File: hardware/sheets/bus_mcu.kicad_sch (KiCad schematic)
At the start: 38 parts, among them M1 Core2350B (0MB PSRAM), U10 74HCT163, U11 74HCT163, U12 74HCT165, U13 74LVC245A, U14 74HCT244, U15 74HCT244, U16 74HCT244, U17 74HCT04, U2 74LVC245A, U3 74LVC245A, U4 74LVC245A, U5 74LVC245A, U6 74LVC245A, U7 74HCT163, U8 74HCT163, U9 74HCT163

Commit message: Fix all medium design-review findings (M1-M8)
- M1: Supervisor link moved to GPIO4/5 (real UART1 pair); POST -> GPIO6-15
- M2: CNT_RUN = LD0.LD1.LD2 gates every '163 CEP (load-cascade hazard)
- M3: ~WR / IO-M pruned to cpu_core-internal; DRQ2/3 pulled + noted;
  doc S5.2 "as built: 48/48" + S16 updated
- M4: true XT-IDE rev-2 map (A0<->A3 swap): data 0x300, latch 0x301,
  CS1 0x307/0x30F, drive DA0 = bus A3 - matches XTIDE UB "rev 2" type
- M5: COM4 -> bus IRQ2 line (IRQ9 via AT redirect); IRQ10/11/14/15 marked
  off-header; ~REFRESH added to mxbus ISA_CTRL; questions-sidecar superseded
- M6: card_isatest clock tree on unswitched V5RAW (spec S8)
- M7: card_isatest IRQ2-8/DRQ1-3 idle pull-downs (spec S4/S9)
- M8: com_port JP1 selects 16550 RX source (DB9 vs TTL console); 5V note

Rebuilt motherboard + cards; structural ERC = 0; netlist-verified.
Fix log in hardware/notes/design-review-2026-07-03.md (batch 3).

Co-Authored-By: Claude Fable 5 <noreply@anthropic.com>
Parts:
- added R14, R15: 10k, symbol Device:R
- added U18: 74HCT08, symbol mini-xt:74HCT08
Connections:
- net +5V: now also U18.14 (VCC); no longer U10.7 (CEP), U11.7 (CEP), U7.7 (CEP), U8.7 (CEP), U9.7 (CEP)
- net CNT_LD0: now also U18.1 (P1)
- net CNT_LD1: now also U18.2 (P2)
- net CNT_LD2: now also U18.5 (P5)
- net DRQ2: now also R14.2
- net DRQ3: now also R15.2
- net GND: now also R14.1, R15.1, U18.10 (P10), U18.12 (P12), U18.13 (P13), U18.7 (GND), U18.9 (P9)
- new net CNT_LD01: U18.3 (P3), U18.4 (P4)
- new net CNT_RUN: U10.7 (CEP), U11.7 (CEP), U18.6 (P6), U7.7 (CEP), U8.7 (CEP), U9.7 (CEP)
- no-connect marks 50 -> 52
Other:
- note added: "DMA ch2/3 + raw ~WR/IO-M are NOT wired to the MCU (48-GPIO budget, S5.2): DACK2/3 parked high, DRQ2/3 low. First candidates for a second '165/'595 if sidecar DMA is ever needed."

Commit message: JLCPCB sourcing pass: verify pinouts, LCSC part numbers, SMD build
Custom-symbol verification (open-questions Q5 resolved):
- MAX3241 symbol was wrong on nearly every pin and used MAX3243-style
  control names; regenerated to the real SSOP-28 pinout (SHDN#/EN#/
  R1OUTB/R2OUTB) and com_port rewired -- EN# must be GROUNDED (the old
  ~FORCEON-high would have disabled the receivers on real silicon)
- DS12C887 symbol wrong on 4 pins (DS=17, RESET#=18, IRQ#=19, SQW=23)

Sourcing (every part checked against the JLC DB; ~45 line items):
- New tools/parts.py maps (lib_id, value) -> LCSC; build.py applies it as
  an 'LCSC Part Num' property on every component (384 across the project)
- Sheets stay generic; stock-forced substitutions bound in the map:
  '374->'574 (parallel rewired), '163->'161, '157->HC157 (+HCT-buffered
  3.3V selects, I0/I1 swapped), '02->HC02, TCM809->MCP809, 2N3904->MMBT3904
- bus_mcu address counters moved to the 3.3V domain (HC161 on 3V3_BUS,
  loaded from MCU-side MD0-7; HCT244s read the 3.3V outputs at TTL Vih)
- 14.318 XOs are 3.3V-only parts: powered from 3V3, squared up via spare
  HCT gates (cpu_core U13, card_isatest U19)
- COM baud reference is now a 1.8432MHz crystal on the 16C550's XIN/XOUT
  (3.3V-only oscillators vs a 5V-only soft card)
- Supervisor QSPI header replaced with a real W25Q128JVSIQ
- Socket policy (fab installs sockets): V20 DIP-40, SRAM DIP-32 (no 5V
  512Kx8 SRAM at JLC at all), DS12C887 DIP-24, female headers for modules

Docs: CLAUDE.md fabrication-constraints section (SMD, 100x100mm, generic-
symbols rule, voltage-domain rule); README + hardware/README fab notes;
notes/jlcpcb-sourcing.md (decisions, thin-stock flags, not-at-JLC list);
stale questions-sidecar.md collapsed to its supersession record.

Rebuilt motherboard + cards: structural ERC 0, byte-identical rebuilds.

Co-Authored-By: Claude Fable 5 <noreply@anthropic.com>
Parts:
- removed C1: 100nF, symbol Device:C
- removed R2: 10k, symbol Device:R
- added C10: 100nF, symbol Device:C
- added R15: 10k, symbol Device:R
- added U17: 74HCT04, symbol mini-xt:74HCT04
- C1: renamed from C2; LCSC Part Num (none) -> C14663
- C11: renamed from U17; value 74HCT04 -> 100nF; symbol mini-xt:74HCT04 -> Device:C; LCSC Part Num (none) -> C14663
- C2: renamed from C3; value 10uF -> 100nF; LCSC Part Num (none) -> C14663
- C3: renamed from C6; value 100nF -> 10uF; LCSC Part Num (none) -> C15850
- C6: renamed from C7; LCSC Part Num (none) -> C14663
- C7: renamed from C8; LCSC Part Num (none) -> C14663
- C8: renamed from C9; LCSC Part Num (none) -> C14663
- C9: renamed from C10; LCSC Part Num (none) -> C14663
- M1: LCSC Part Num (none) -> C2897411
- R1: LCSC Part Num (none) -> C25804
- R10: renamed from R11; LCSC Part Num (none) -> C25804
- R11: renamed from R12; LCSC Part Num (none) -> C25804
- R12: renamed from R13; LCSC Part Num (none) -> C25804
- R13: renamed from R14; LCSC Part Num (none) -> C25804
- R14: renamed from R15; LCSC Part Num (none) -> C25804
- R2: renamed from R3; LCSC Part Num (none) -> C25804
- R3: renamed from R4; LCSC Part Num (none) -> C25804
- R4: renamed from R5; LCSC Part Num (none) -> C25804
- R5: renamed from R6; LCSC Part Num (none) -> C25804
- R6: renamed from R7; LCSC Part Num (none) -> C25804
- R7: renamed from R8; LCSC Part Num (none) -> C25804
- R8: renamed from R9; LCSC Part Num (none) -> C25804
- R9: renamed from R10; LCSC Part Num (none) -> C25804
- U10, U11, U7, U8, U9: value 74HCT163 -> 74HC161; LCSC Part Num (none) -> C5610
- U12: LCSC Part Num (none) -> C456131
- U13, U2, U3, U4, U5, U6: LCSC Part Num (none) -> C6082
- U14, U15, U16: LCSC Part Num (none) -> C5978
- U18: value 74HCT08 -> 74HC08; LCSC Part Num (none) -> C5593
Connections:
- net 3V3_BUS is gone; now on net GND: C1.1, C2.1, C3.1, C6.1, M1.50 (3V3), U13.1 (A->B), U13.20 (VCC), U2.20 (VCC), U3.20 (VCC), U4.20 (VCC), U5.20 (VCC), U6.20 (VCC)
- net +3V3: now also C8.1; no longer C7.1
- net +5V: now also R13.1, R3.1, C10.1, U17.14 (VCC); no longer C11.14 (VCC), C8.1, C9.1, R11.1, U10.1 (~{MR}), U10.16 (VCC), U11.1 (~{MR}), U11.16 (VCC), U18.14 (VCC), U7.1 (~{MR}), U7.10 (CET), U7.16 (VCC), U8.1 (~{MR}), U8.16 (VCC), U9.1 (~{MR}), U9.16 (VCC)
- net D0: no longer U11.3 (D0), U7.3 (D0), U9.3 (D0)
- net D1: no longer U11.4 (D1), U7.4 (D1), U9.4 (D1)
- net D2: no longer U11.5 (D2), U7.5 (D2), U9.5 (D2)
- net D3: no longer U11.6 (D3), U7.6 (D3), U9.6 (D3)
- net D4: no longer U10.3 (D0), U8.3 (D0)
- net D5: no longer U10.4 (D1), U8.4 (D1)
- net D6: no longer U10.5 (D2), U8.5 (D2)
- net D7: no longer U10.6 (D3), U8.6 (D3)
- net DRQ2: now also R14.2; no longer R13.2
- net DRQ3: now also R15.2; no longer R14.2
- net GND: now also C11.1, C11.2, C7.1, C9.1, R11.1, U10.1 (~{MR}), U10.16 (VCC), U11.1 (~{MR}), U11.16 (VCC), U18.14 (VCC), U7.1 (~{MR}), U7.10 (CET), U7.16 (VCC), U8.1 (~{MR}), U8.16 (VCC), U9.1 (~{MR}), U9.16 (VCC), C10.2, R15.1, U17.7 (GND); no longer C11.7 (GND), R13.1, R3.1
- net HLDA: now also U17.1 (P1); no longer C11.1 (P1)
- net IOCHRDY: now also R2.2
- net IRQ2: now also R4.2; no longer R3.2
- net IRQ3: now also R5.2; no longer R4.2
- net IRQ4: now also R6.2; no longer R5.2
- net IRQ5: now also R7.2; no longer R6.2
- net IRQ6: now also R8.2; no longer R7.2
- net IRQ7: now also R9.2; no longer R8.2
- net IRQ8: now also R10.2; no longer R9.2
- net IRQ9: now also R11.2; no longer R10.2
- net MD0: now also U11.3 (D0), U7.3 (D0), U9.3 (D0)
- net MD1: now also U11.4 (D1), U7.4 (D1), U9.4 (D1)
- net MD2: now also U11.5 (D2), U7.5 (D2), U9.5 (D2)
- net MD3: now also U11.6 (D3), U7.6 (D3), U9.6 (D3)
- net MD4: now also U10.3 (D0), U8.3 (D0)
- net MD5: now also U10.4 (D1), U8.4 (D1)
- net MD6: now also U10.5 (D2), U8.5 (D2)
- net MD7: now also U10.6 (D3), U8.6 (D3)
- net ~{DACK2}: now also R12.2; no longer R11.2
- net ~{DACK3}: now also R13.2; no longer R12.2
- net ~{HLDA}: now also U17.2 (P2); no longer C11.2 (P2)
- net ~{IOCHCK}: now also R3.2; no longer R2.2
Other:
- moved on the sheet: C1, C2, C3, C6, C7, C8, C9, R10, R11, R12, R13, R14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

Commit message: Design review 2026-07-11: rail protection, decoupling, wiring fixes
Protection:
- Sidecar +5V now feeds through a 2A polyfuse into +5V_ISA with an
  SMBJ5.0A clamp + 22uF bulk (a faulted ISA card trips its own fuse
  instead of dropping the board; back-fed voltage is clamped).
- USB-C VBUS enters through a 3A polyfuse with an SMBJ5.0A on +5V
  (backstop for the CFG1 9-20V failure mode). CH224K gains a 1uF VDD
  cap; its PG routes to Supervisor GPIO16 as PD_PG. Buck output
  doubled to 2x22uF, 10uF at VIN, extra rail bulk.
- Supervisor USB-A host port: 27R series termination (RP2040
  requirement), USBLC6-2SC6 ESD array, 100uF VBUS bulk.
- Video: HDMI +5V fused (500mA), HPD sensed on GPIO41, 100R series on
  VGA sync. TMDS ESD array deferred to layout (no symbol).
- card_isatest: V5RAW bulk, Q1 gate soft-start cap, TVS on DUT rail.

Wiring fixes:
- SPKR had no driver anywhere (netlist: 1 node). Bus MCU GPIO22
  reassigned from the diagnostics-only bus-CLK sense to SPKR; bus_mcu
  drops CLK from its interface. Doc 5.2 updated.
- bus_mcu C8 decoupled +3V3, a rail that sheet never uses -> 3V3_BUS.
- Storage IRQ5 was push-pull (permanently driven when idle) -> 2N7002
  + gated '125 tri-state, same convention as the LPT IRQ7 stage.
- MAX3241 pump caps resized to the 5V datasheet values (47nF/330nF).
- LPT DB25 status inputs get 4.7k pull-ups (floated with no printer).
- Audio line-out gets a 100R series isolator before the jack.

Best practices:
- Decoupling to ~1x100nF per IC on every sheet + bulk per board
  (cpu_core 7->16 incl. the naked 3.3V oscillator, storage 4->11,
  parallel 6->13, rtc/com/video/bus_mcu/card_isatest similar).
- All floating spare CMOS inputs tied ('00/'74/'157/'02/'04/'125
  sections across cpu_core, bus_mcu, rtc, storage, card_isatest).

Sourcing: new parts mapped in parts.py with JLC-verified LCSC numbers;
Power_Protection lib registered in the tools; TPS563200 stock alert
(4 pcs left at JLC) flagged in parts.py + jlcpcb-sourcing.md. All
decisi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
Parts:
- removed C1: 100nF, symbol Device:C
- removed R2: 10k, symbol Device:R
- added C10, C12, C13, C14, C15, C16, C17: 100nF, symbol Device:C
- added R15: 10k, symbol Device:R
- C2: renamed from C3; value 10uF -> 100nF; LCSC Part Num C15850 -> C14663
- C3: renamed from C6; value 100nF -> 10uF; LCSC Part Num C14663 -> C15850
- renumbered C2 to C1, C7 to C6, C8 to C7, C9 to C8, C10 to C9, R11 to R10, R12 to R11, R13 to R12, R14 to R13, R15 to R14, R3 to R2, R4 to R3, R5 to R4, R6 to R5, R7 to R6, R8 to R7, R9 to R8, R10 to R9
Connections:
- net +3V3 is gone; now on net GND: C7.1
- net +5V: now also R13.1, R3.1, C10.1, C12.1, C13.1, C14.1, C15.1; no longer C9.1, R11.1
- net DRQ2: now also R14.2; no longer R13.2
- net DRQ3: now also R15.2; no longer R14.2
- net GND: now also C9.1, R11.1, U17.11 (P11), U17.13 (P13), U17.3 (P3), U17.5 (P5), U17.9 (P9), C10.2, C12.2, C13.2, C14.2, C15.2, C16.1, C16.2, C17.1, C17.2, R15.1; no longer R13.1, R3.1
- net IOCHRDY: now also R2.2
- net IRQ2: now also R4.2; no longer R3.2
- net IRQ3: now also R5.2; no longer R4.2
- net IRQ4: now also R6.2; no longer R5.2
- net IRQ5: now also R7.2; no longer R6.2
- net IRQ6: now also R8.2; no longer R7.2
- net IRQ7: now also R9.2; no longer R8.2
- net IRQ8: now also R10.2; no longer R9.2
- net IRQ9: now also R11.2; no longer R10.2
- net ~{DACK2}: now also R12.2; no longer R11.2
- net ~{DACK3}: now also R13.2; no longer R12.2
- net ~{IOCHCK}: now also R3.2; no longer R2.2
- net CLK renamed SPKR
- no-connect marks 52 -> 47
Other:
- moved on the sheet: C1, C2, C3, C6, C7, C8, C9, R10, R11, R12, R13, R14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

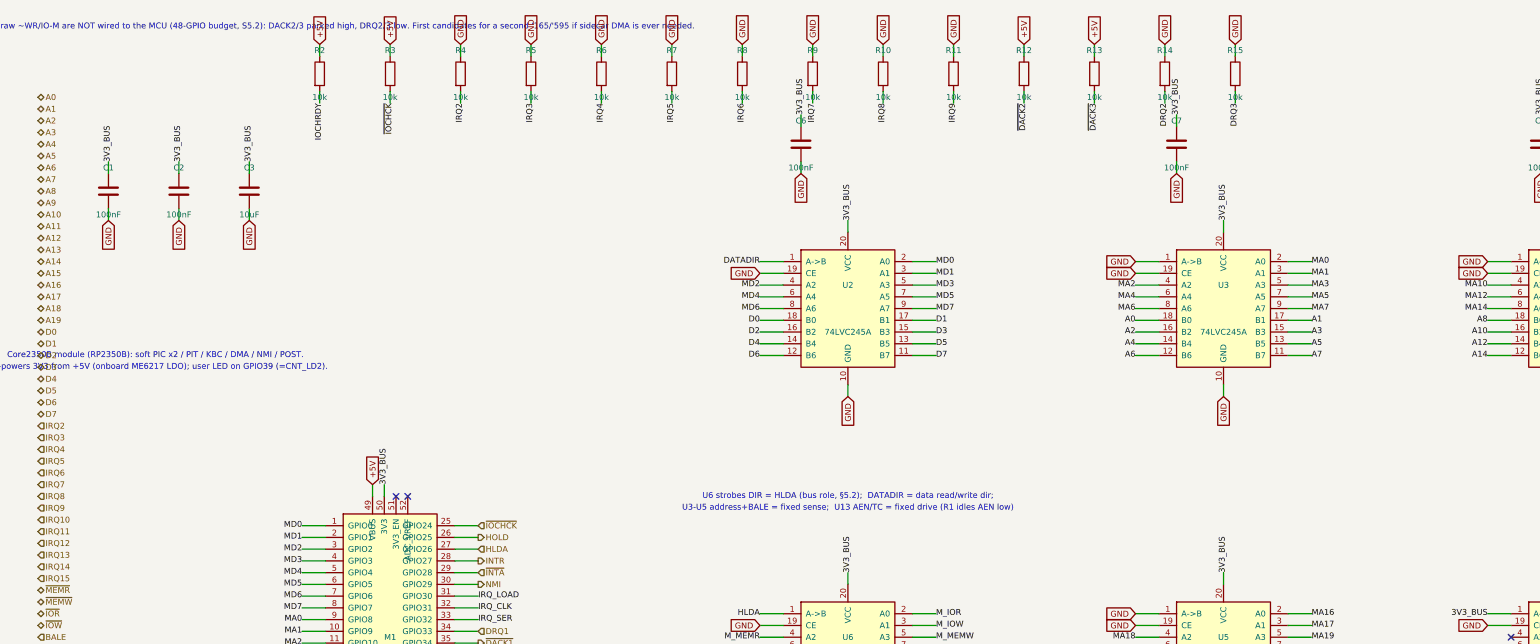
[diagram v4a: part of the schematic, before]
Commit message: Core2350B sites: VBUS diode-OR + Hi-Z shifter parking
The Waveshare Core2350B has NO diode between its on-module USB connector
and its VBUS pin (vendor schematic, hardware/Core2350B.pdf) -- with both
module sites tied straight to +5V, plugging a PC in for firmware flashing
would back-power the whole board (board off) or parallel two hard 5V
supplies (board on).

- D1 (SS34) per site, Pico-style: +5V -> anode, module VBUS -> cathode
  (nets VBUS_MCU / VBUS_VID). USB flashing powers only the module; a
  running board never back-drives the PC port. The ME6217 LDO has ample
  headroom at ~4.7 V in.
- Hi-Z parking so a BOOTSEL/pre-init MCU (all GPIO Hi-Z) never drives the
  5 V bus through the shifters: bus_mcu R16-R18 (DATADIR B->A sense --
  U2's enable is hard-grounded; M_TC low; HLDA low, defining U6's
  direction when the V20 side is unpowered); video R32-R37 (DOE/AOE_*/
  RDY_OE to 3V3_VID = active-low enables parked off, DDIR low). Before
  this, those controls floated whenever firmware wasn't driving them.

Doc 12 gains a "module-USB flashing is safe" bullet; decisions logged in
questions-bus_mcu.md / questions-video.md. card_video inherits the diode
and pulls automatically.

Verified: motherboard + cards rebuild with zero structural ERC; netlist
shows VBUS_MCU/VBUS_VID = {module VBUS, D cathode} only, and each parking
net = {module GPIO, resistor, shifter pin} (HLDA additionally spans its
12-node handoff group with R218).

Co-Authored-By: Claude Fable 5 <noreply@anthropic.com>
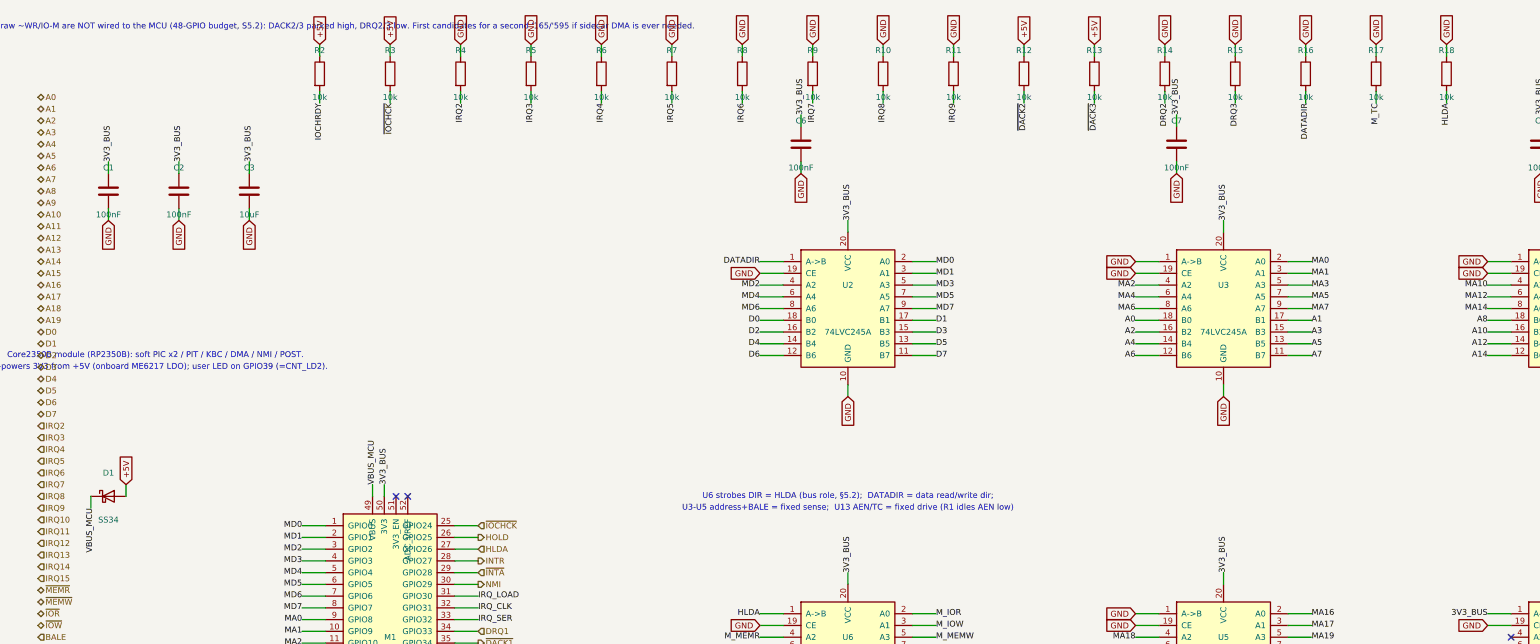
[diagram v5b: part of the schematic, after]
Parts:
- removed C1, C11, C2, C6: 100nF, symbol Device:C
- removed C3: 10uF, symbol Device:C
- removed R1, R2: 10k, symbol Device:R
- added C14, C15, C16, C17: 100nF, symbol Device:C
- added R15, R16, R17, R18: 10k, symbol Device:R
- added U17: 74HCT04, symbol mini-xt:74HCT04
- added U2: 74LVC245A, symbol mini-xt:74LVC245A
- added U7: 74HC161, symbol mini-xt:74HCT163
- C11: renamed from U17; value 74HCT04 -> 100nF; symbol mini-xt:74HCT04 -> Device:C; LCSC Part Num C672096 -> C14663
- C3: renamed from C9; value 100nF -> 10uF; LCSC Part Num C14663 -> C15850
- D1: renamed from U2; value 74LVC245A -> SS34; symbol mini-xt:74LVC245A -> Device:D_Schottky; LCSC Part Num C6082 -> (none)
- R1: renamed from U7; value 74HC161 -> 10k; symbol mini-xt:74HCT163 -> Device:R; LCSC Part Num C5610 -> C25804
- renumbered C7 to C1, C15 to C10, C16 to C12, C17 to C13, C8 to C2, C10 to C6, C12 to C7, C13 to C8, C14 to C9, R11 to R10, R12 to R11, R13 to R12, R14 to R13, R15 to R14, R3 to R2, R4 to R3, R5 to R4, R6 to R5, R7 to R6, R8 to R7, R9 to R8, R10 to R9
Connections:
- net +5V: now also C12.1, C13.1, D1.2 (A), R13.1, R3.1, C14.1, C15.1, U17.14 (VCC); no longer C11.14 (VCC), C6.1, C7.1, C8.1, C9.1, M1.49 (VBUS), R11.1
- net CA0: now also U7.14 (Q0); no longer R1.14 (Q0)
- net CA1: now also U7.13 (Q1); no longer R1.13 (Q1)
- net CA2: now also U7.12 (Q2); no longer R1.12 (Q2)
- net CA3: now also U7.11 (Q3); no longer R1.11 (Q3)
- net CNT_CLK: now also U7.2 (CP); no longer R1.2 (CP)
- net CNT_LD0: now also U7.9 (~{PE}); no longer R1.9 (~{PE})
- net CNT_RUN: now also U7.7 (CEP); no longer R1.7 (CEP)
- net CNT_TC0: now also U7.15 (TC); no longer R1.15 (TC)
- net D0: now also U2.18 (B0); no longer D1.18 (B0)
- net D1: now also U2.17 (B1); no longer D1.17 (B1)
- net D2: now also U2.16 (B2); no longer D1.16 (B2)
- net D3: now also U2.15 (B3); no longer D1.15 (B3)
- net D4: now also U2.14 (B4); no longer D1.14 (B4)
- net D5: now also U2.13 (B5); no longer D1.13 (B5)
- net D6: now also U2.12 (B6); no longer D1.12 (B6)
- net D7: now also U2.11 (B7); no longer D1.11 (B7)
- net DATADIR: now also R16.2, U2.1 (A->B); no longer D1.1 (A->B)
- net DRQ2: now also R14.2; no longer R13.2
- net DRQ3: now also R15.2; no longer R14.2
- net GND: now also C11.1, C11.2, C6.1, C7.1, C8.1, C9.1, R1.2, R11.1, C14.2, C15.2, C16.1, C16.2, C17.1, C17.2, R15.1, R16.1, R17.1, R18.1, U17.11 (P11), U17.13 (P13), U17.3 (P3), U17.5 (P5), U17.7 (GND), U17.9 (P9), U2.10 (GND), U2.19 (CE), U2.20 (VCC), U7.1 (~{MR}), U7.10 (CET), U7.16 (VCC), U7.8 (GND); no longer C11.11 (P11), C11.13 (P13), C11.3 (P3), C11.5 (P5), C11.7 (GND), C11.9 (P9), C12.1, C13.1, D1.10 (GND), D1.19 (CE), D1.20 (VCC), R1.1 (~{MR}), R1.10 (CET), R1.16 (VCC), R1.8 (GND), R13.1, R3.1
- net HLDA: now also R18.2, U17.1 (P1); no longer C11.1 (P1)
- net IOCHRDY: now also R2.2
- net IRQ2: now also R4.2; no longer R3.2
- net IRQ3: now also R5.2; no longer R4.2
- net IRQ4: now also R6.2; no longer R5.2
- net IRQ5: now also R7.2; no longer R6.2
- net IRQ6: now also R8.2; no longer R7.2
- net IRQ7: now also R9.2; no longer R8.2
- net IRQ8: now also R10.2; no longer R9.2
- net IRQ9: now also R11.2; no longer R10.2
- net MD0: now also U2.2 (A0), U7.3 (D0); no longer D1.2 (A0), R1.3 (D0)
- net MD1: now also U2.3 (A1), U7.4 (D1); no longer D1.3 (A1), R1.4 (D1)
- net MD2: now also U2.4 (A2), U7.5 (D2); no longer D1.4 (A2), R1.5 (D2)
- net MD3: now also U2.5 (A3), U7.6 (D3); no longer D1.5 (A3), R1.6 (D3)
- net MD4: now also U2.6 (A4); no longer D1.6 (A4)
- net MD5: now also U2.7 (A5); no longer D1.7 (A5)
- net MD6: now also U2.8 (A6); no longer D1.8 (A6)
- net MD7: now also U2.9 (A7); no longer D1.9 (A7)
- net M_AEN: now also R1.1
- net M_TC: now also R17.2
- net ~{DACK2}: now also R12.2; no longer R11.2
- net ~{DACK3}: now also R13.2; no longer R12.2
- net ~{HLDA}: now also U17.2 (P2); no longer C11.2 (P2)
- net ~{IOCHCK}: now also R3.2; no longer R2.2
- new net VBUS_MCU: D1.1 (K), M1.49 (VBUS)
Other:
- moved on the sheet: C1, C10, C12, C13, C2, C3, C6, C7, C8, C9, R10, R11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
